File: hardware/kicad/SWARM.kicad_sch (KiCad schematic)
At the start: 1 part

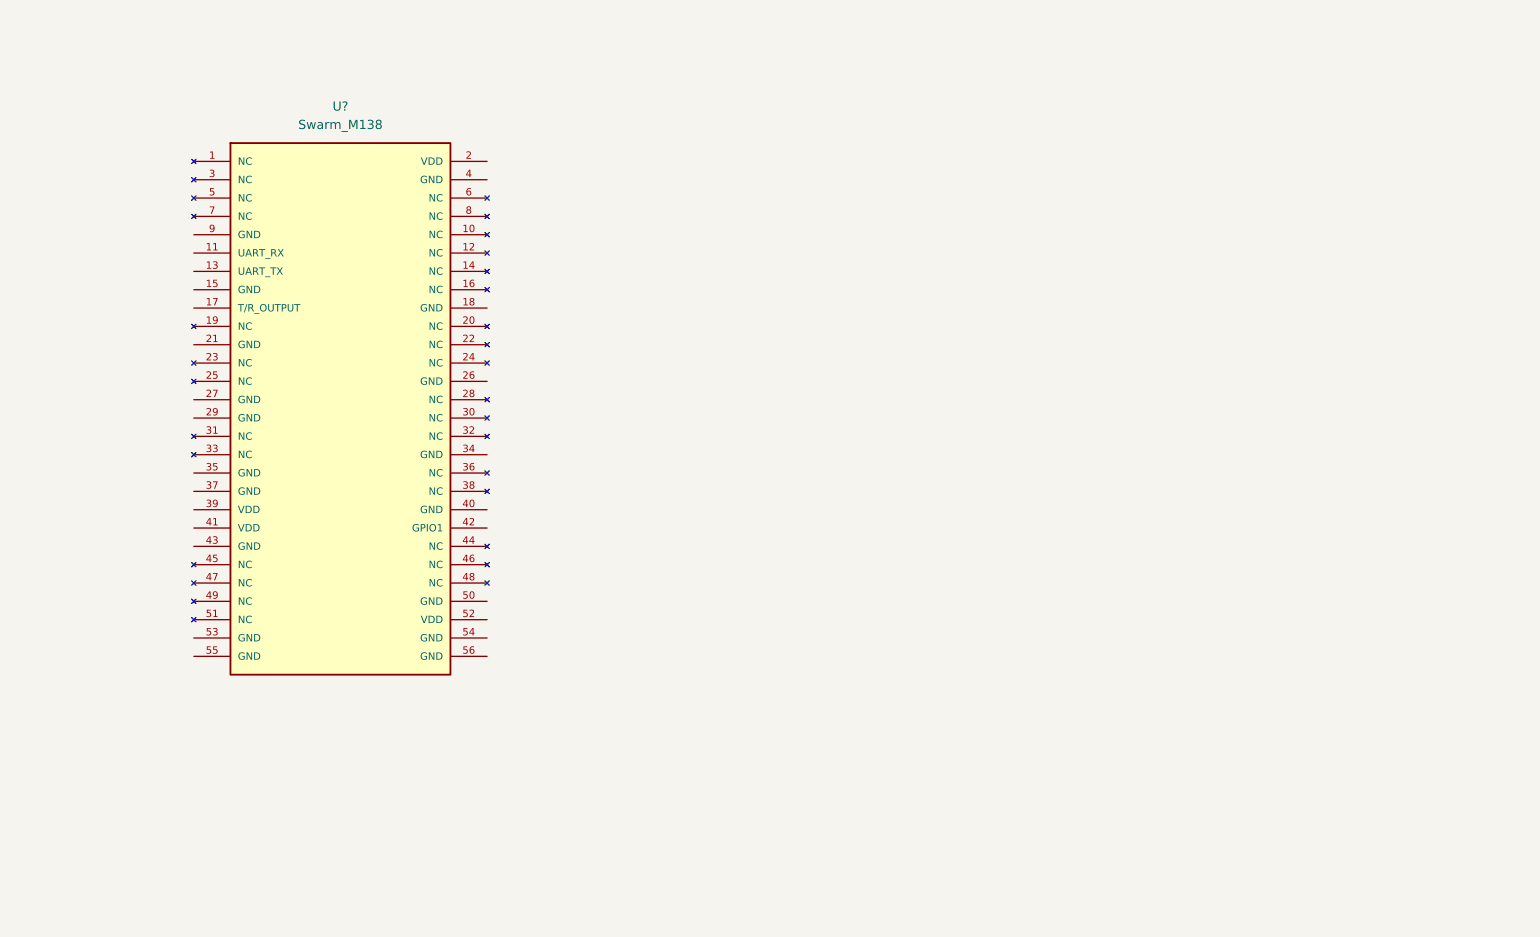
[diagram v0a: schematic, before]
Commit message: update schematic
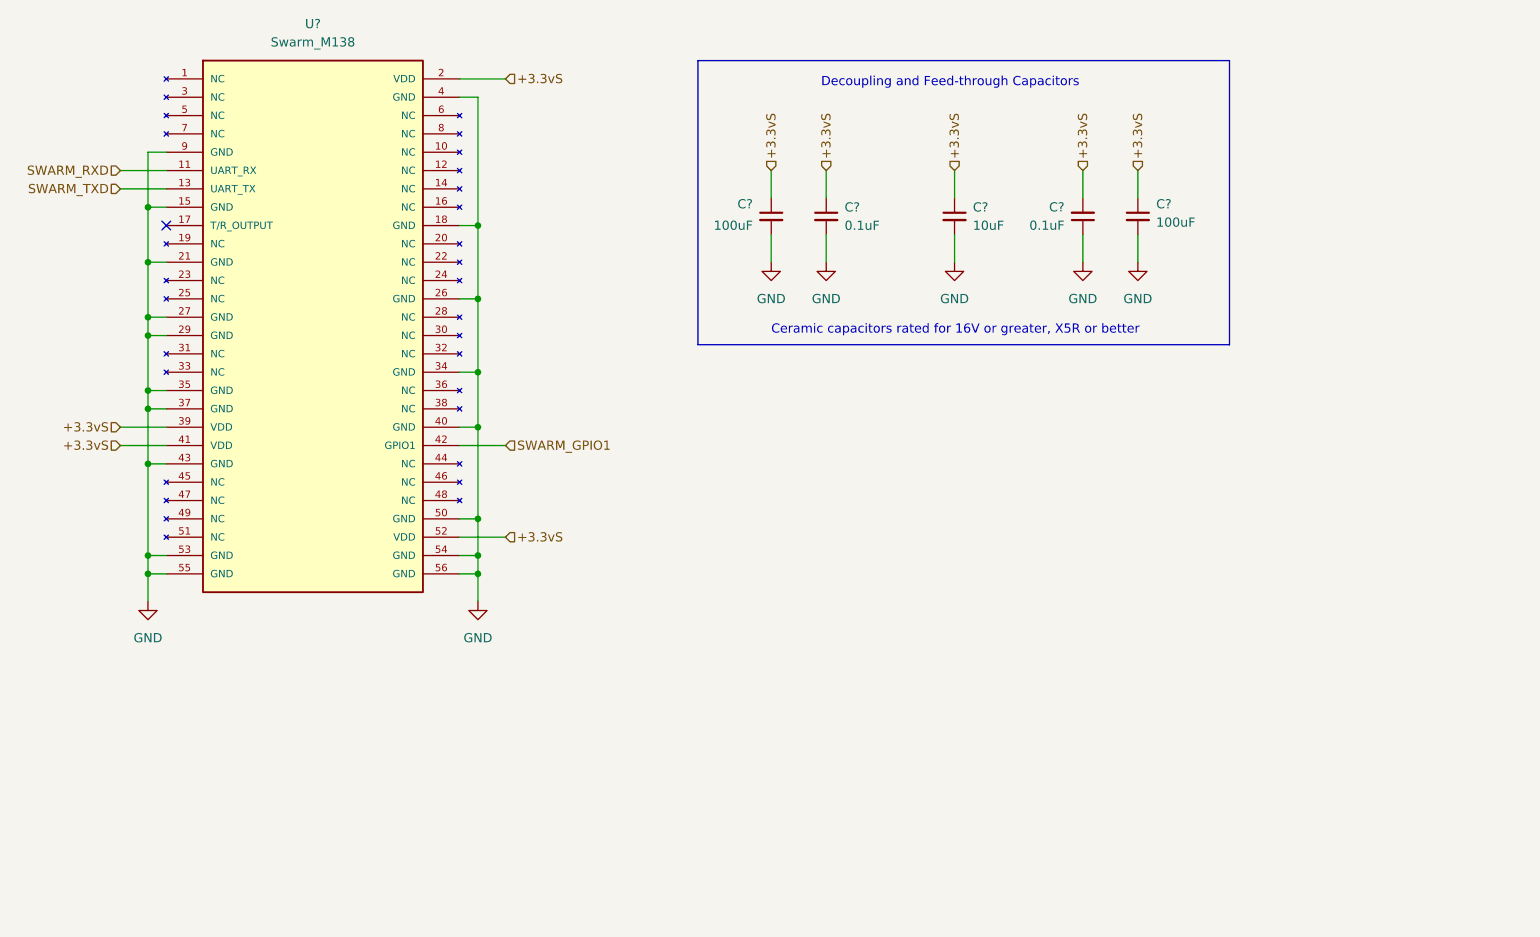
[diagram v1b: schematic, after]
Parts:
- added C? (x2): 0.1uF, symbol Device:C_Small
- added C?: 10uF, symbol Device:C_Small
- added C? (x2): 100uF, symbol Device:C_Small
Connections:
- net SWARM_RXD: now reaches U?.11 (UART_RX)
- net SWARM_TXD: now reaches U?.13 (UART_TX)
- net GND: now reaches U?.15 (GND)
- net GND: now also U?.18 (GND), U?.21 (GND), U?.26 (GND), U?.27 (GND), U?.29 (GND), U?.34 (GND), U?.35 (GND), U?.37 (GND), U?.4 (GND), U?.40 (GND), U?.43 (GND), U?.50 (GND), U?.53 (GND), U?.54 (GND), U?.55 (GND), U?.56 (GND), U?.9 (GND), C?.1, C?.2, C?.2, C?.2, C?.2
- net +3.3vS: now reaches U?.2 (VDD)
- net +3.3vS: now also U?.39 (VDD), U?.41 (VDD), U?.52 (VDD), C?.1, C?.1, C?.1, C?.1, C?.2
- net SWARM_GPIO1: now reaches U?.42 (GPIO1)
- no-connect marks 0 -> 1
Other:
- note added: "Ceramic capacitors rated for 16V or greater, X5R or better"
- note added: "Decoupling and Feed-through Capacitors"
- moved on the sheet: U?

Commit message: update pcb design
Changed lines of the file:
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@@
     (effects (font (size 1.27 1.27)) (justify left))
   )
-  (hierarchical_label "SWARM_GPIO1" (shape input) (at 100.33 85.09 0)
+  (hierarchical_label "SWARM_GPIO1" (shape bidirectional) (at 100.33 85.09 0)
     (effects (font (size 1.27 1.27)) (justify left))
   )
@@
     (effects (font (size 1.27 1.27)) (justify right))
   )
-  (hierarchical_label "SWARM_TXD" (shape input) (at 46.99 49.53 180)
+  (hierarchical_label "SWARM_TXD" (shape output) (at 46.99 49.53 180)
     (effects (font (size 1.27 1.27)) (justify right))
   )

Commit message: initial pcb design
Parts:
- C26, C30: renamed from C?; footprint (none) -> Capacitor_SMD:C_1210_3225Metric
- C27, C29: renamed from C?; footprint (none) -> Capacitor_SMD:C_0402_1005Metric
- C28: renamed from C?; footprint (none) -> Capacitor_SMD:C_0805_2012Metric
- gave numbers to parts that had none: 1
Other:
- note added: "SWARM Satellite Transceiver Module"
- moved on the sheet: C26, C27, C28, C29, C30, U12
